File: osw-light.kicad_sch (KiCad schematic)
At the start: 53 parts, among them J2 USB_C_Receptacle_USB2.0, Q1 2N7002, SW1 SW_Push, SW2 SW_Push, SW4 SW_Push, SW5 SW_Push, U1 RV-8523-C3, U10 XC6209, U13 XC6209, U2 BME280, U3 ESP32-PICO-MINI-02, U4 GC9A01_IPS_display, U5 BQ24230RGT, U6 CH340E, U7 LSM303C

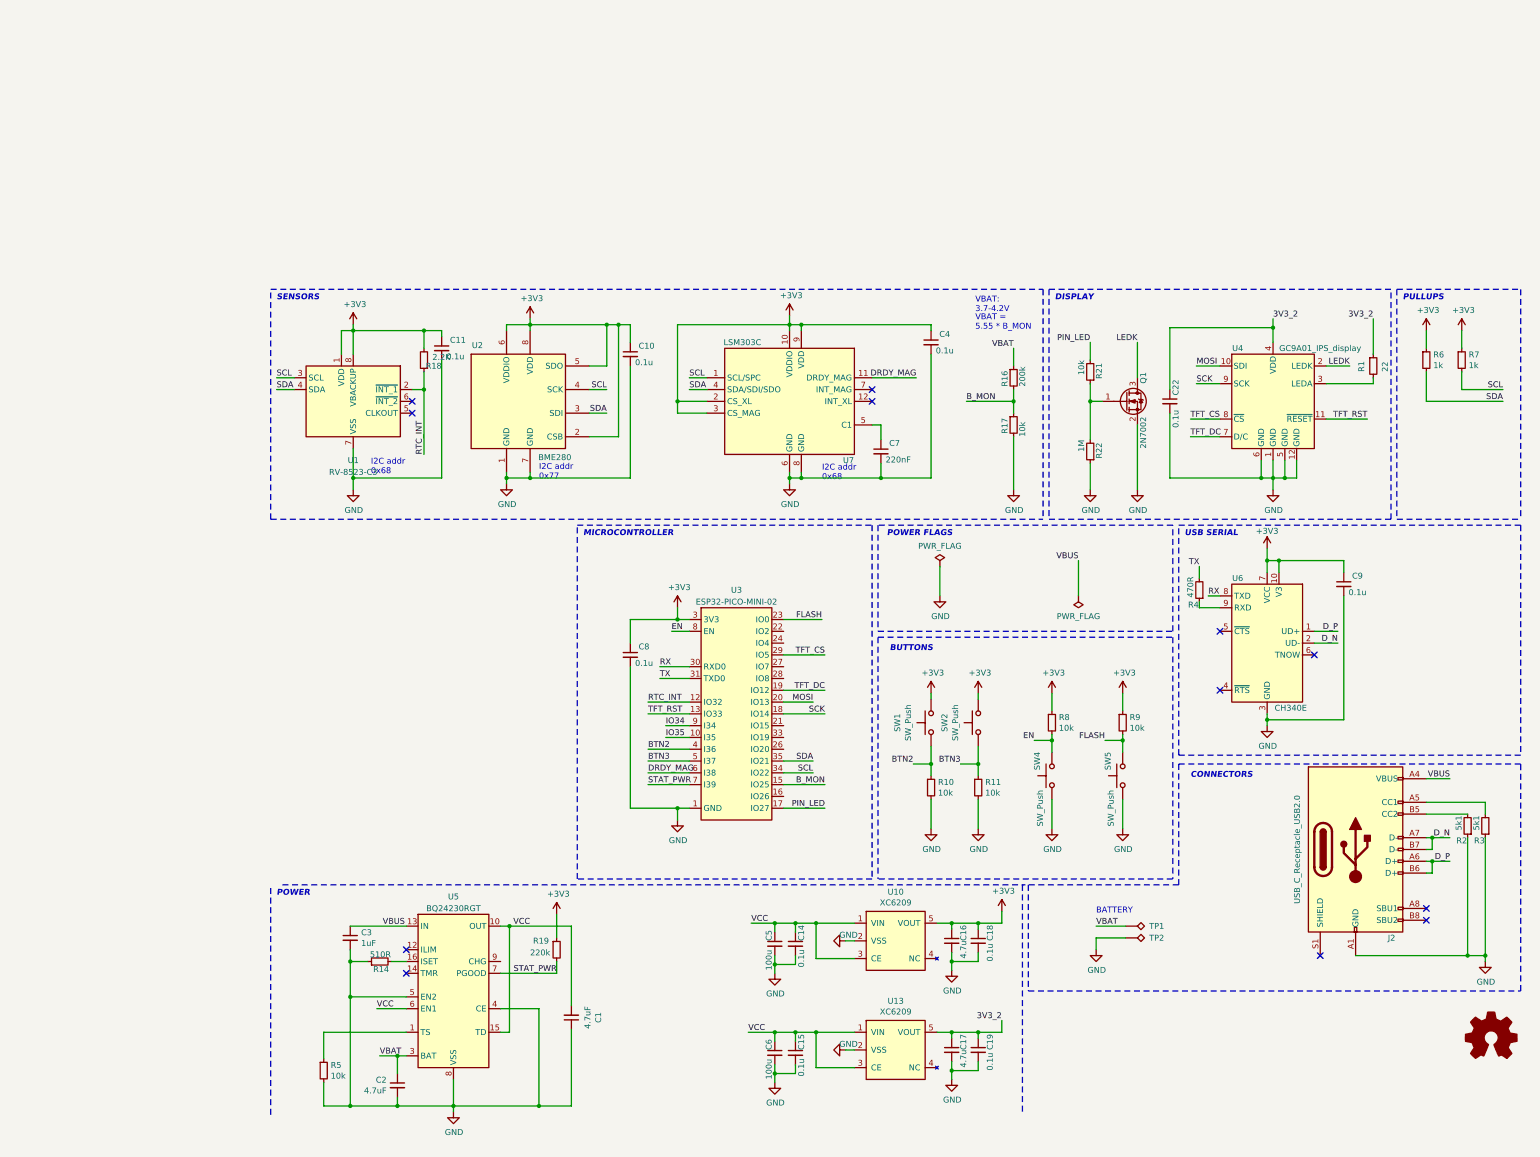
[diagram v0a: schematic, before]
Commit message: Started work on a Rev2 of this fork
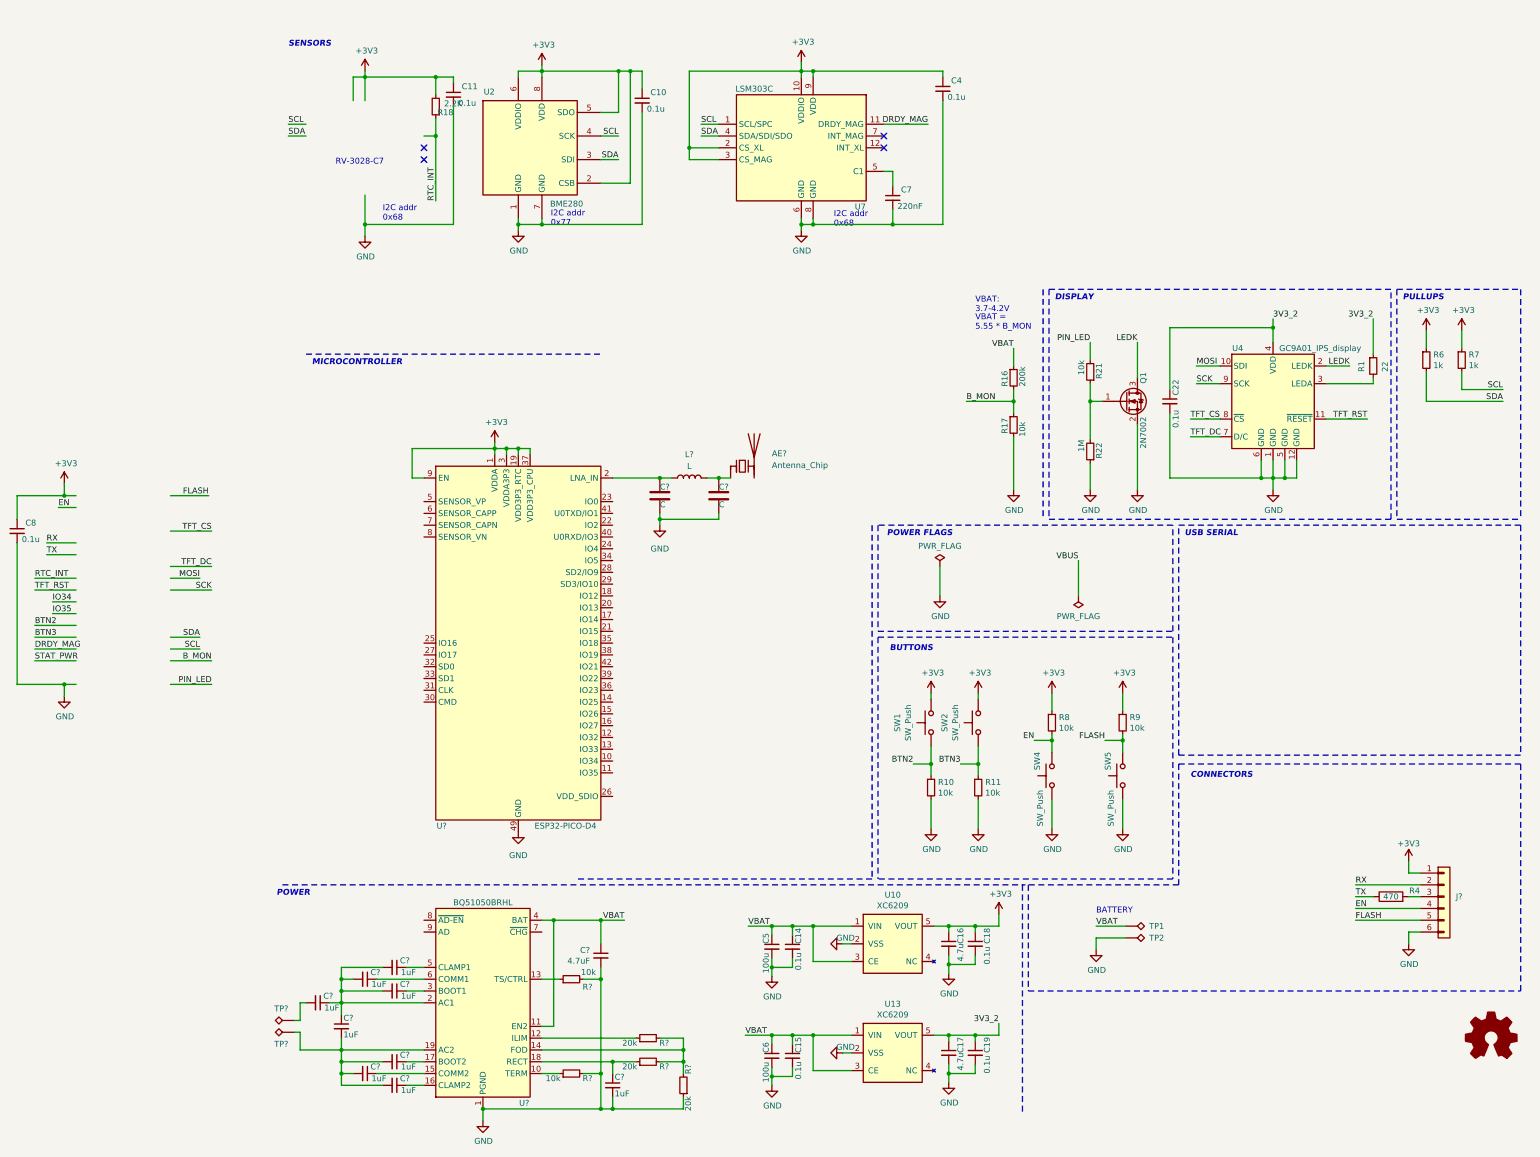
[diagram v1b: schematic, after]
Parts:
- removed C1, C2: 4.7uF, Capacitor_SMD:C_0603_1608Metric, symbol Device:C_Small
- removed C3: 1uF, Capacitor_SMD:C_0603_1608Metric, symbol Device:C_Small
- removed C9: 0.1u, Capacitor_SMD:C_0603_1608Metric, symbol Device:C_Small
- removed J2: USB_C_Receptacle_USB2.0, Connector_USB:USB_C_Receptacle_GCT_USB4085, symbol Connector:USB_C_Receptacle_USB2.0
- removed R14: 510R, Resistor_SMD:R_0603_1608Metric, symbol Device:R_Small
- removed R19: 220k, Resistor_SMD:R_0603_1608Metric, symbol Device:R_Small
- removed R2, R3: 5k1, Resistor_SMD:R_0603_1608Metric, symbol Device:R_Small
- removed R4: 470R, Resistor_SMD:R_0603_1608Metric, symbol Device:R_Small
- removed R5: 10k, Resistor_SMD:R_0603_1608Metric, symbol Device:R_Small
- removed U1: RV-8523-C3, Package_SON:RTC_SMD_MicroCrystal_C3_2.5x3.7mm, symbol Timer_RTC:RV-8523-C3
- removed U3: ESP32-PICO-MINI-02, open-Smartwatch:ESP32-PICO-MINI-02, symbol open-Smartwatch:ESP32-PICO-MINI-02
- removed U5: BQ24230RGT, Package_DFN_QFN:VQFN-16-1EP_3x3mm_P0.5mm_EP1.68x1.68mm_ThermalVias, symbol Power_Management:BQ24230RGT
- removed U6: CH340E, open-Smartwatch:MSOP-10_3x3mm_P0.5mm, symbol open-Smartwatch:CH340E
- added AE?: Antenna_Chip, symbol Device:Antenna_Chip
- added C? (x2): C, symbol Device:C
- added C? (x9): 1uF, Capacitor_SMD:C_0603_1608Metric, symbol Device:C_Small
- added C?: 4.7uF, Capacitor_SMD:C_0603_1608Metric, symbol Device:C_Small
- added J?: Conn_01x06, symbol Connector_Generic:Conn_01x06
- added L?: L, symbol Device:L
- added R4: 470, symbol Device:R
- added R? (x2): 10k, Resistor_SMD:R_0603_1608Metric, symbol Device:R_Small
- added R? (x3): 20k, Resistor_SMD:R_0603_1608Metric, symbol Device:R_Small
- added TP? (x2): BATT-VCC, TestPoint:TestPoint_Pad_3.0x3.0mm, symbol Connector:TestPoint_Alt
- added U?: ESP32-PICO-D4, Package_DFN_QFN:QFN-48-1EP_7x7mm_P0.5mm_EP5.3x5.3mm, symbol RF_Module:ESP32-PICO-D4
- added U?: BQ51050BRHL, Package_DFN_QFN:Texas_VQFN-RHL-20, symbol Battery_Management:BQ51050BRHL
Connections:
- net VCC is gone; now on net VBAT: C14.1, C15.1, C5.1, C6.1, U10.1 (VIN), U10.3 (CE), U13.1 (VIN), U13.3 (CE)
- net +3V3: now also J?.1 (Pin_1), U?.1 (VDDA), U?.19 (VDD3P3_RTC), U?.3 (VDDA3P3), U?.37 (VDD3P3_CPU), U?.4 (VDDA3P3), U?.43 (VDDA), U?.46 (VDDA), U?.9 (EN)
- net EN: now also J?.4 (Pin_4)
- net FLASH: now also J?.5 (Pin_5)
- net GND: now also C?.2, C?.2, C?.2, C?.2, J?.6 (Pin_6), R?.1, R?.2, R?.2, U?.1 (PGND), U?.20 (PGND), U?.21 (PGND), U?.49 (GND)
- net RX: now also J?.2 (Pin_2)
- net TX: now also R4.1
- net VBAT: now also C?.1, U?.11 (EN2), U?.4 (BAT)
- new net: C?.1, L?.1, U?.2 (LNA_IN)
- new net: C?.1, U?.5 (CLAMP1)
- new net: C?.1, C?.1, C?.2, C?.2, C?.2, U?.2 (AC1)
- new net: AE?.1 (FEED), C?.1, L?.2
- new net: C?.2, C?.2, C?.2, C?.2, TP?.1, U?.19 (AC2)
- new net: R?.1, U?.10 (TERM)
- new net: C?.1, U?.15 (COMM2)
- new net: C?.1, U?.3 (BOOT1)
- new net: C?.2, TP?.1
- new net: C?.1, U?.16 (CLAMP2)
- new net: J?.3 (Pin_3), R4.2
- new net: R?.1, U?.12 (ILIM)
- new net: R?.1, U?.13 (TS/CTRL)
- new net: R?.2, R?.2, R?.2, U?.14 (FOD)
- new net: C?.1, U?.17 (BOOT2)
- new net: C?.1, R?.1, U?.18 (RECT)
- new net: C?.1, U?.6 (COMM1)
- no-connect marks 12 -> 4
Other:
- note added: "RV-3028-C7"
- moved on the sheet: C10, C11, C14, C15, C16, C17, C18, C19, C4, C5, C6, C7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

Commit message: Initial traces for Rev2
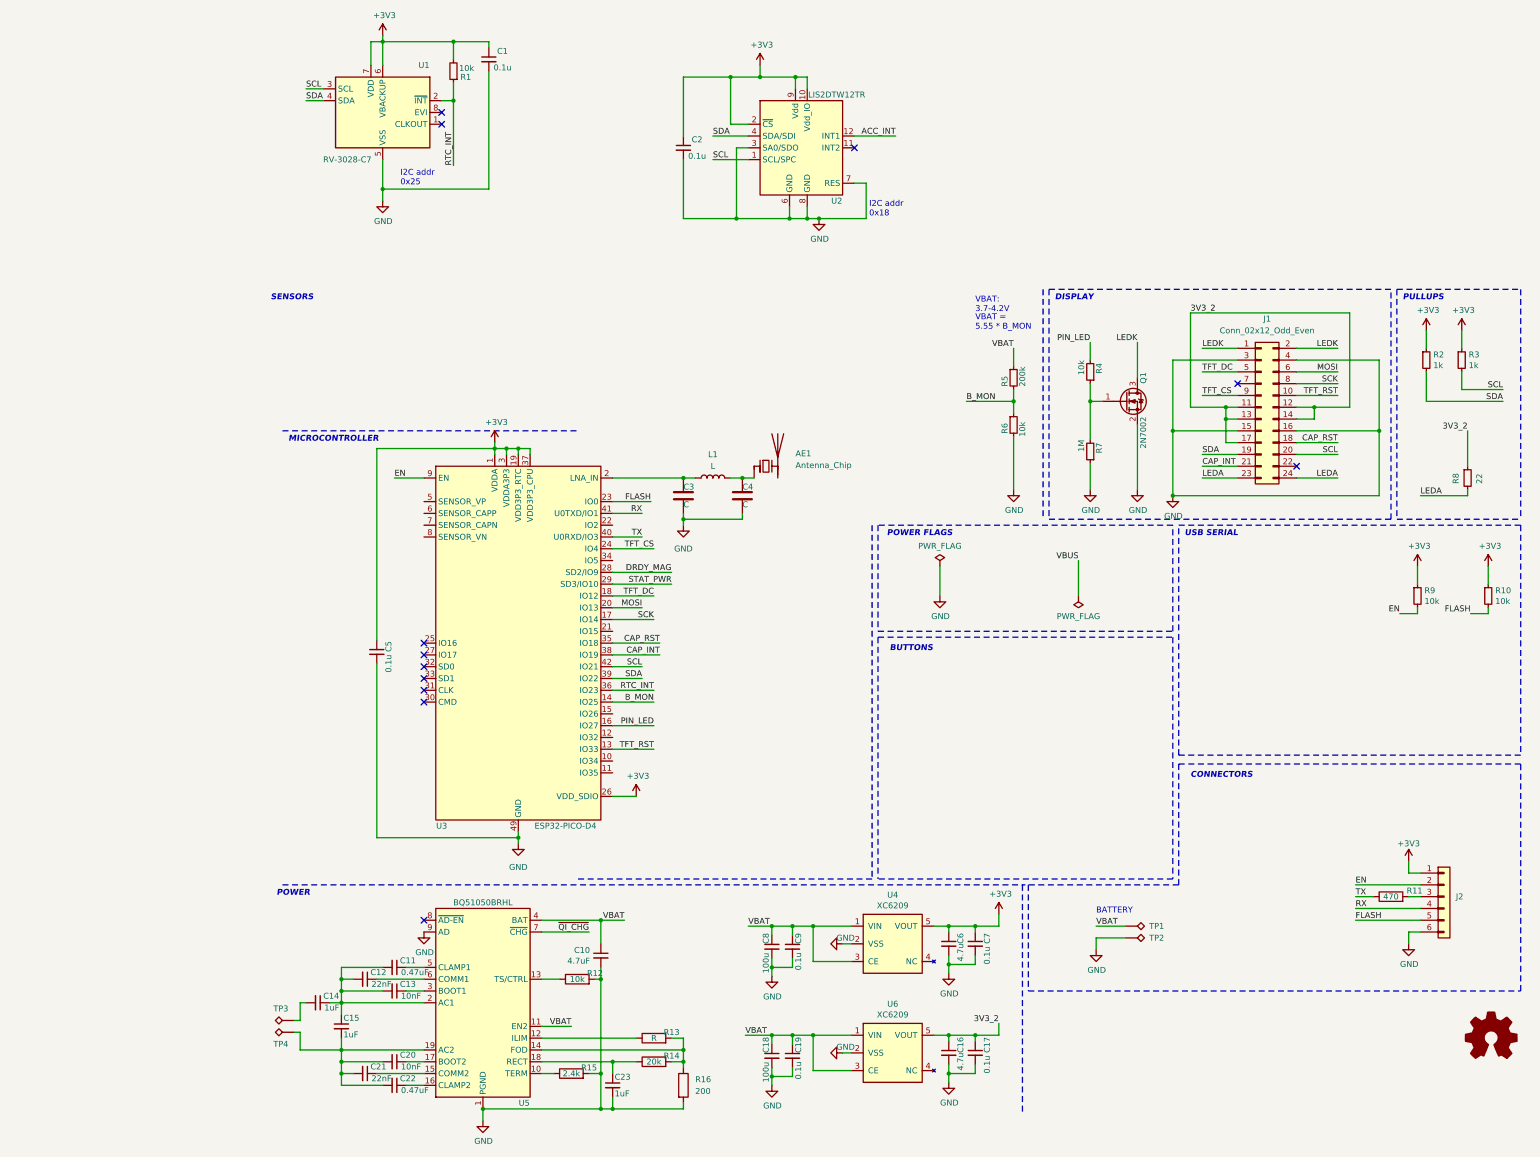
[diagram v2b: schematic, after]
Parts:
- removed C22, C4, C8: 0.1u, Capacitor_SMD:C_0603_1608Metric, symbol Device:C_Small
- removed C7: 220nF, Capacitor_SMD:C_0603_1608Metric, symbol Device:C_Small
- removed R10, R11, R? (x2): 10k, Resistor_SMD:R_0603_1608Metric, symbol Device:R_Small
- removed R? (x3): 20k, Resistor_SMD:R_0603_1608Metric, symbol Device:R_Small
- removed SW1, SW2, SW4, SW5: SW_Push, open-Smartwatch:button_side_smd, symbol Switch:SW_Push
- removed U2: BME280, Package_LGA:Bosch_LGA-8_2.5x2.5mm_P0.65mm_ClockwisePinNumbering, symbol Sensor:BME280
- removed U4: GC9A01_IPS_display, open-Smartwatch:GC9A01_IPS_display, symbol open-Smartwatch:GC9A01_IPS_display_SPI
- removed U7: LSM303C, Package_LGA:LGA-12_2x2mm_P0.5mm, symbol Sensor_Motion:LSM303C
- added C5: 0.1u, Capacitor_SMD:C_0603_1608Metric, symbol Device:C_Small
- added J1: Conn_02x12_Odd_Even, open-Smartwatch:DisplayFlexConnector, symbol Connector_Generic:Conn_02x12_Odd_Even
- added R12: 10k, Resistor_SMD:R_0603_1608Metric, symbol Device:R
- added R13: R, Resistor_SMD:R_0603_1608Metric, symbol Device:R
- added R14: 20k, Resistor_SMD:R_0603_1608Metric, symbol Device:R
- added R15: 2.4k, Resistor_SMD:R_0603_1608Metric, symbol Device:R
- added R16: 200, Resistor_SMD:R_0603_1608Metric, symbol Device:R
- added U1: RV-3028-C7, open-Smartwatch:RTC_SMD_MicroCrystal_C7_1.5x3.2mm, symbol open-Smartwatch:RV-3028-C7
- added U2: LIS2DTW12TR, Package_LGA:LGA-12_2x2mm_P0.5mm, symbol open-Smartwatch:LIS2DTW12TR
- AE1: renamed from AE?; footprint (none) -> RF_Antenna:Johanson_2450AT43F0100
- C11, C22: renamed from C?; value 1uF -> 0.47uF
- C12, C21: renamed from C?; value 1uF -> 22nF
- C13, C20: renamed from C?; value 1uF -> 10nF
- C16: renamed from C17; footprint Capacitor_SMD:C_0603_1608Metric -> Capacitor_SMD:C_0805_2012Metric
- C3, C4: renamed from C?; footprint (none) -> Capacitor_SMD:C_0603_1608Metric
- C6: renamed from C16; footprint Capacitor_SMD:C_0603_1608Metric -> Capacitor_SMD:C_0805_2012Metric
- J2: renamed from J?; footprint (none) -> Connector:Tag-Connect_TC2030-IDC-NL_2x03_P1.27mm_Vertical
- L1: renamed from L?; footprint (none) -> Inductor_SMD:L_0805_2012Metric_Pad1.05x1.20mm_HandSolder
- R1: renamed from R18; value 2.2K -> 10k
- R11: renamed from R4; footprint (none) -> Resistor_SMD:R_0603_1608Metric
- gave numbers to parts that had none: 8
- renumbered C11 to C1, C19 to C17, C6 to C18, C15 to C19, C10 to C2, C18 to C7, C5 to C8, C14 to C9, R9 to R10, R6 to R2, R7 to R3, R21 to R4, R16 to R5, R17 to R6, R22 to R7, R1 to R8, R8 to R9, U10 to U4, U13 to U6
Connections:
- net +3V3: now also U3.26 (VDD_SDIO), C5.1, U1.6 (VBACKUP), U1.7 (VDD), U2.10 (Vdd_IO), U2.2 (~{CS}), U2.9 (Vdd); no longer U3.9 (EN)
- net 3V3_2: now also J1.11 (Pin_11), J1.12 (Pin_12), J1.13 (Pin_13), J1.14 (Pin_14), J1.17 (Pin_17)
- net B_MON: now also U3.14 (IO25)
- net DRDY_MAG: now also U3.28 (SD2/IO9)
- net EN: now also J2.2 (Pin_2), U3.9 (EN); no longer J2.4 (Pin_4)
- net FLASH: now also U3.23 (IO0)
- net GND: now also U5.9 (AD), C5.2, J1.15 (Pin_15), J1.16 (Pin_16), J1.3 (Pin_3), J1.4 (Pin_4), R12.2, R15.2, R16.2, U1.5 (VSS), U2.3 (SA0/SDO), U2.6 (GND), U2.7 (RES), U2.8 (GND)
- net LEDK: now also J1.1 (Pin_1), J1.2 (Pin_2)
- net MOSI: now also U3.20 (IO13), J1.6 (Pin_6)
- net PIN_LED: now also U3.16 (IO27)
- net RTC_INT: now also U3.36 (IO23), U1.2 (~{INT})
- net RX: now also J2.4 (Pin_4), U3.41 (U0TXD/IO1); no longer J2.2 (Pin_2)
- net SCK: now also U3.17 (IO14), J1.8 (Pin_8)
- net SCL: now also U3.42 (IO21), J1.20 (Pin_20), U1.3 (SCL), U2.1 (SCL/SPC)
- net SDA: now also U3.39 (IO22), J1.19 (Pin_19), U1.4 (SDA), U2.4 (SDA/SDI)
- net STAT_PWR: now also U3.29 (SD3/IO10)
- net TFT_CS: now also U3.24 (IO4), J1.9 (Pin_9)
- net TFT_DC: now also U3.18 (IO12), J1.5 (Pin_5)
- net TFT_RST: now also U3.13 (IO33), J1.10 (Pin_10)
- net TX: now also U3.40 (U0RXD/IO3)
- net LEDA: now reaches R8.2
- net LEDA: now also J1.23 (Pin_23), J1.24 (Pin_24)
- net CAP_RST: now reaches U3.35 (IO18)
- net CAP_RST: now also J1.18 (Pin_18)
- net CAP_INT: now reaches U3.38 (IO19)
- net CAP_INT: now also J1.21 (Pin_21)
- net at U5.10 (TERM): now also R15.1
- net at U5.12 (ILIM): now also R13.1
- net at U5.13 (TS/CTRL): now also R12.1
- net at U5.14 (FOD): now also R13.2, R14.2, R16.1
- net at C23.1, U5.18 (RECT): now also R14.1
- net ~{QI_CHG}: now reaches U5.7 (~{CHG})
- new net ACC_INT: U2.12 (INT1)
- no-connect marks 4 -> 12
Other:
- note added: "I2C addr 0x18"
- note added: "I2C addr 0x25"
- note removed: "I2C addr 0x68"
- note removed: "I2C addr 0x77"
- note removed: "RV-3028-C7"
- moved on the sheet: AE1, C1, C2, C3, C4, L1, R1, R10, R8, R9

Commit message: Near finished with Rev2 Design
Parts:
- C10, C14, C15: footprint Capacitor_SMD:C_0603_1608Metric -> Capacitor_SMD:C_0805_2012Metric
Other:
- note added: "MISC"
- note added: "POWER FLAGS and CONNECTORS"
- note added: "QI"
- note removed: "BUTTONS"
- note removed: "CONNECTORS"
- note removed: "POWER"
- note removed: "POWER FLAGS"
- note removed: "USB SERIAL"
- moved on the sheet: AE1, C1, C10, C11, C12, C13, C14, C15, C2, C20, C21, C22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

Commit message: Started work on a Rev3
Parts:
- removed C2: 0.1u, Capacitor_SMD:C_0603_1608Metric, symbol Device:C_Small
- removed U1: RV-3028-C7, open-Smartwatch:RTC_SMD_MicroCrystal_C7_1.5x3.2mm, symbol open-Smartwatch:RV-3028-C7
- removed U2: LIS2DTW12TR, Package_LGA:LGA-12_2x2mm_P0.5mm, symbol open-Smartwatch:LIS2DTW12TR
- added U1: MCP7940N-xMS, Package_SO:MSOP-8_3x3mm_P0.65mm, symbol Timer_RTC:MCP7940N-xMS
- added Y1: 32.768khz, Crystal:Crystal_SMD_3215-2Pin_3.2x1.5mm, symbol Device:Crystal_Small
- C14: value 1uF -> 44nF
- C15: value 1uF -> 470pF
- R13: value R -> 412
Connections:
- net +3V3: now also U1.3 (VBAT), U1.8 (VCC)
- net GND: now also U1.4 (VSS)
- net RTC_INT: now also U1.7 (MFP)
- net SCL: now also U1.6 (SCL)
- net SDA: now also U1.5 (SDA)
- new net: U1.1 (X1), Y1.2
- new net: U1.2 (X2), Y1.1
- no-connect marks 12 -> 9
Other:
- note removed: "I2C addr 0x18"
- moved on the sheet: R1
